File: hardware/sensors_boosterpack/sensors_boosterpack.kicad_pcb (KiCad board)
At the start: 2 copper layers, 3 parts, among them J1 Conn_01x08, J2 Conn_01x40, J3 Conn_01x08

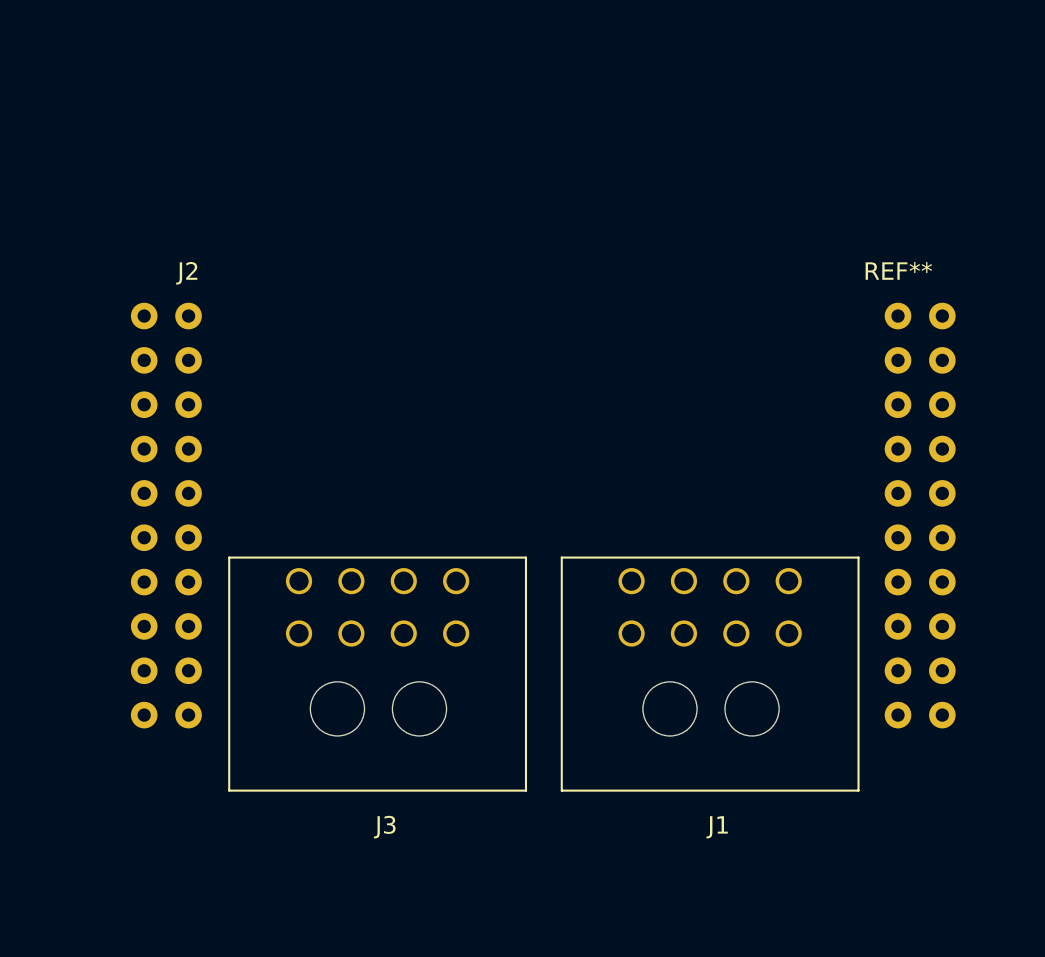
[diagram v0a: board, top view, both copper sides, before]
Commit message: Fixed hole sizes (ugh)
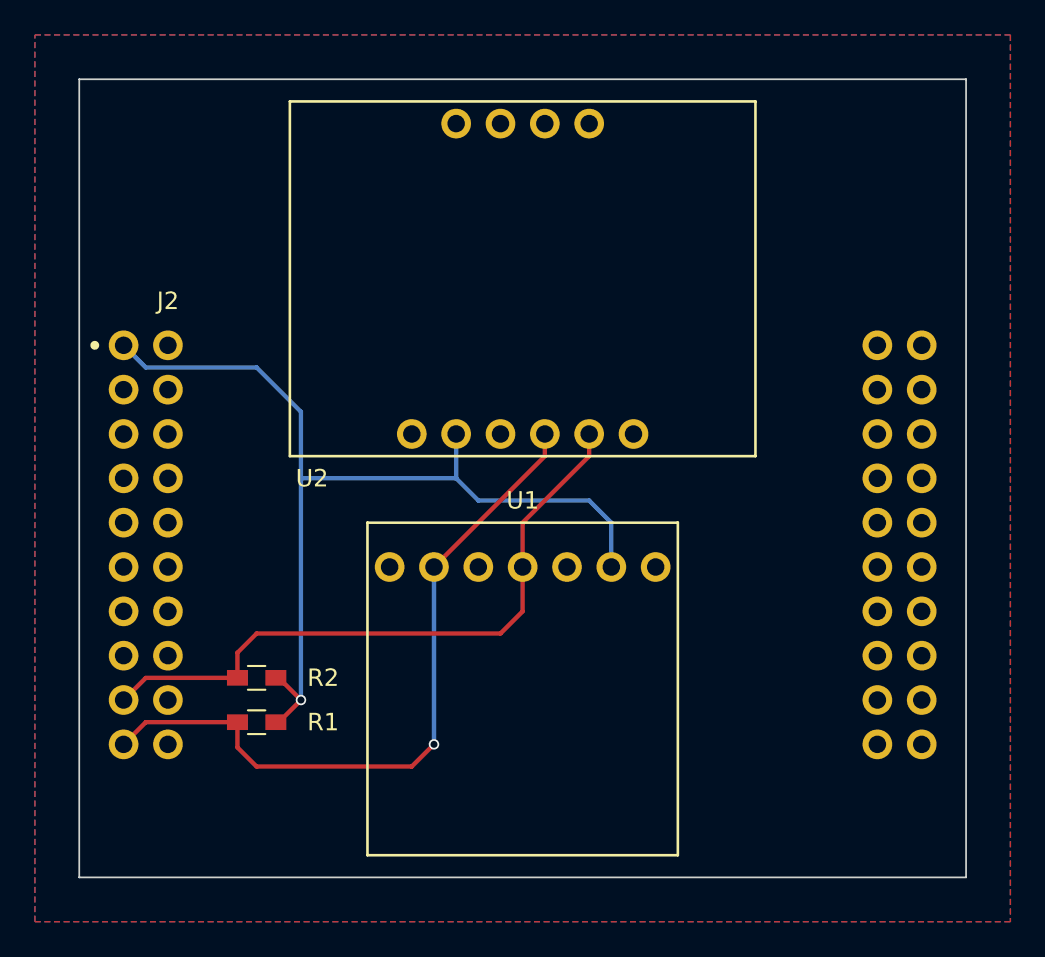
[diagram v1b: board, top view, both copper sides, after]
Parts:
- removed J1, J3: Conn_01x08, Connectors_Molex:Molex_Microfit3_Header_02x04_Angled_43045-080x
- added R1: 4.7k, Resistors_SMD:R_0603_HandSoldering, F.Cu at (154.9, 105.4)
- added R2: 4.7k, Resistors_SMD:R_0603_HandSoldering, F.Cu at (154.9, 102.9)
- added U1: adafruit_bmp280, capstone_board_components:adafruit_bmp280, F.Cu at (179.1, 94.0)
- added U2: adafruit_bno055, capstone_board_components:adafruit_bno055, F.Cu at (163.8, 88.9)
- moved J2 2.05 mm to (147.3, 106.7)
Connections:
- J2 pad 16: /RST -> Net-(J2-Pad16)
- J2 pad 2: /TRIG -> Net-(J2-Pad2)
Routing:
- net +3V3: track 0.00 -> 56.1 mm, vias 0 -> 1
- net /SDA: track 0.00 -> 41.1 mm, vias 0 -> 1
- net /SCL: track 0.00 -> 37.5 mm
- added copper zone on B.Cu, net GND
- added copper zone on F.Cu, net GND
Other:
- board outline added: 50.8 x 45.7 mm
- rule pad_to_mask_clearance: 0.2 -> 0
- board text added: "ECE Capstone 2018 Sensor BoosterPack Ag Despopoulos Version 2"
